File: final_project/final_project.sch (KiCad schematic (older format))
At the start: 35 parts, among them J1 USB_microB_2040002-1, J2 Arduino_ICSP, J3 Conn_01x15_Male, J4 Conn_01x15_Male, U1 FT232RQ, U2 MCP1702T-5002E_CB, U3 TPS2113ADRBR, U4 ATMEGA328PB-MNR, Y1 Crystal

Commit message: full footprints
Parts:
- U2: footprint (none) -> Package_TO_SOT_SMD:SOT-23
- Y1: footprint (none) -> final:CSTNE
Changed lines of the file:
@@
 F 0 "U2" H 4800 2365 50  0000 C CNN
 F 1 "MCP1702T-5002E_CB" H 4800 2274 50  0000 C CNN
-F 2 "" H 4800 2100 50  0001 C CNN
+F 2 "Package_TO_SOT_SMD:SOT-23" H 4800 2100 50  0001 C CNN
 F 3 "" H 4800 2100 50  0001 C CNN
 	1    4800 2000
@@
 F 0 "Y1" V 8654 5331 50  0000 L CNN
 F 1 "Crystal" V 8745 5331 50  0000 L CNN
-F 2 "" H 8700 5200 50  0001 C CNN
+F 2 "final:CSTNE" H 8700 5200 50  0001 C CNN
 F 3 "" H 8700 5200 50  0001 C CNN
 	1    8700 5200

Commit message: add rn symbol
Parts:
- added U?: RN4871, symbol final_project-rescue:RN4871
- S1: footprint (none) -> Button_Switch_SMD:SW_SPST_B3U-1000P
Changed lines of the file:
@@
 F 0 "S1" H 7048 5346 50  0000 L CNN
 F 1 "SW" H 7048 5255 50  0000 L CNN
-F 2 "" V 7050 5400 60  0001 C CNN
+F 2 "Button_Switch_SMD:SW_SPST_B3U-1000P" V 7050 5400 60  0001 C CNN
 F 3 "" V 7050 5400 60  0001 C CNN
 	1    7000 5300
@@
 	1    0    0    -1
 $EndComp
+$Comp
+L final_project-rescue:RN4871 U?
+U 1 1 5CA7B34A
+P 13150 5100
+F 0 "U?" H 13150 5915 50  0000 C CNN
+F 1 "RN4871" H 13150 5824 50  0000 C CNN
+F 2 "" H 13150 5950 50  0001 C CNN
+F 3 "" H 13150 5950 50  0001 C CNN
+	1    13150 5100
+	1    0    0    -1
+$EndComp

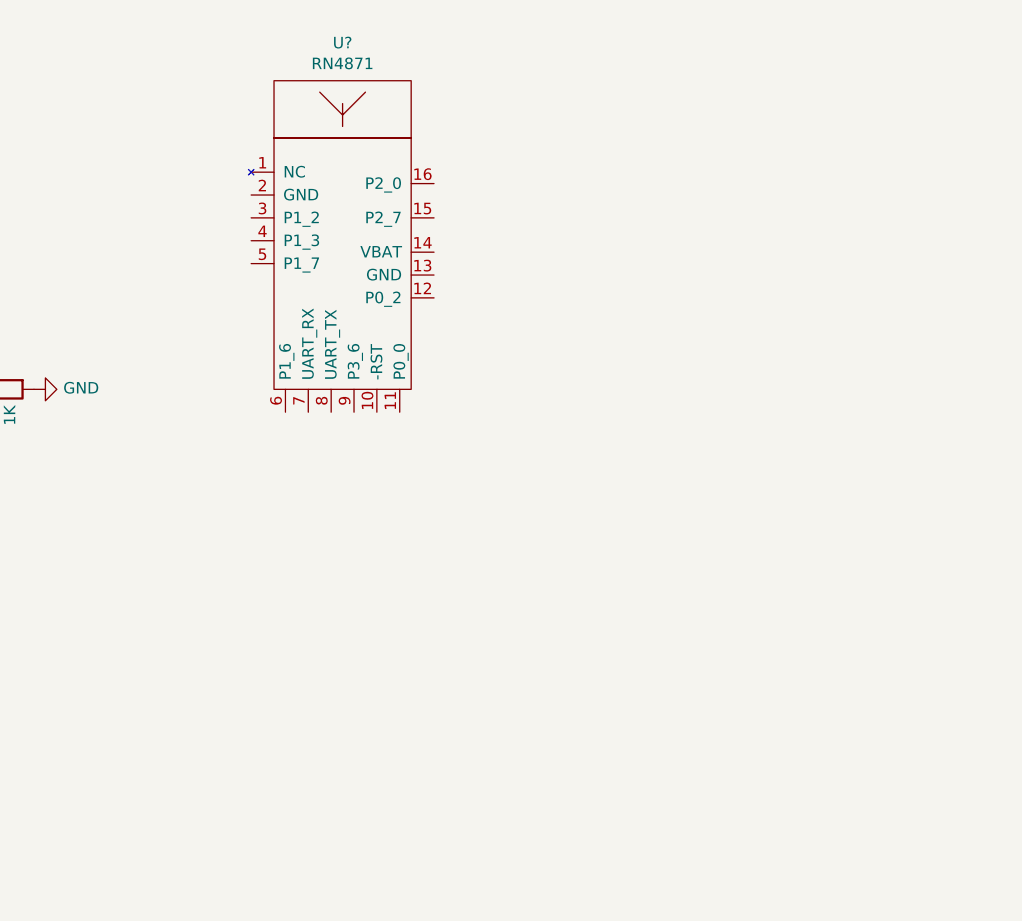
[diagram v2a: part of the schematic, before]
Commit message: rn4871 application circuit
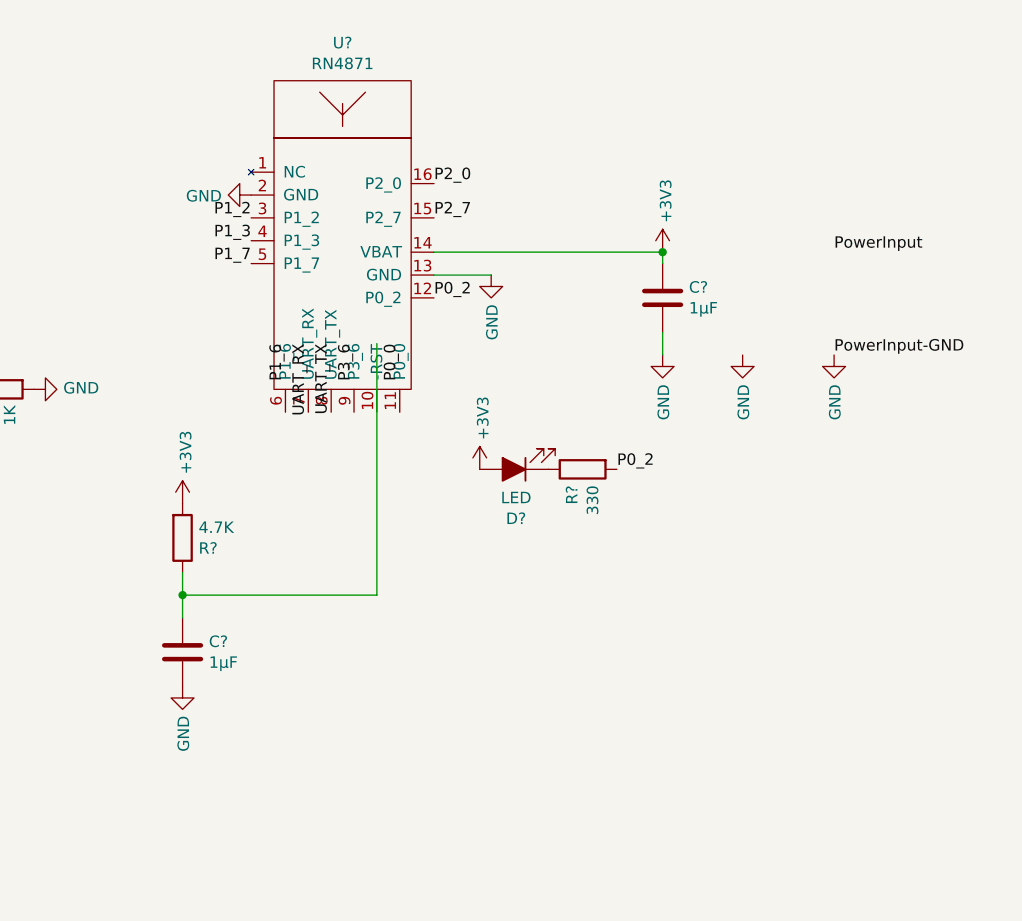
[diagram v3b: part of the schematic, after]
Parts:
- added C? (x2): 1µF, Capacitor_SMD:C_0603_1608Metric, symbol Device:C
- added D?: LED, LED_SMD:LED_0805_2012Metric, symbol Device:LED_ALT
- added R?: 4.7K, Resistor_SMD:R_0603_1608Metric, symbol Device:R
- added R?: 330, Resistor_SMD:R_0603_1608Metric, symbol Device:R
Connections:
- net labels added: P0_0, P0_2, P1_2, P1_3, P1_6, P1_7, P2_0, P2_7, P3_6, PowerInput, PowerInput-GND, UART_RX, UART_TX
- wire segments 98 -> 106
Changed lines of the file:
@@
 	1    0    0    -1
 $EndComp
+$Comp
+L power:GND #PWR?
+U 1 1 5CA7F048
+P 12750 4950
+F 0 "#PWR?" H 12750 4700 50  0001 C CNN
+F 1 "GND" V 12755 4822 50  0000 R CNN
+F 2 "" H 12750 4950 50  0001 C CNN
+F 3 "" H 12750 4950 50  0001 C CNN
+	1    12750 4950
+	0    1    1    0
+$EndComp
+$Comp
+L power:GND #PWR?
+U 1 1 5CA84F44
+P 14550 5650
+F 0 "#PWR?" H 14550 5400 50  0001 C CNN
+F 1 "GND" V 14555 5522 50  0000 R CNN
+F 2 "" H 14550 5650 50  0001 C CNN
+F 3 "" H 14550 5650 50  0001 C CNN
+	1    14550 5650
+	1    0    0    -1
+$EndComp
+Text Label 12750 5050 2    50   ~ 0
+P1_2
+Text Label 12750 5150 2    50   ~ 0
+P1_3
+Text Label 12750 5250 2    50   ~ 0
+P1_7
+Text Label 12900 5600 3    50   ~ 0
+P1_6
+Text Label 13000 5600 3    50   ~ 0
+UART_RX
+Text Label 13100 5600 3    50   ~ 0
+UART_TX
+Text Label 13200 5600 3    50   ~ 0
+P3_6
+Text Label 13400 5600 3    50   ~ 0
+P0_0
+$Comp
+L Device:C C?
+U 1 1 5CA99BD0
+P 12450 6950
+F 0 "C?" H 12565 6996 50  0000 L CNN
+F 1 "1µF" H 12565 6905 50  0000 L CNN
+F 2 "Capacitor_SMD:C_0603_1608Metric" H 12488 6800 50  0001 C CNN
+F 3 "~" H 12450 6950 50  0001 C CNN
+	1    12450 6950
+	1    0    0    -1
+$EndComp
+$Comp
+L power:+3V3 #PWR?
+U 1 1 5CA99BD6
+P 12450 6300
+F 0 "#PWR?" H 12450 6150 50  0001 C CNN
+F 1 "+3V3" V 12465 6428 50  0000 L CNN
+F 2 "" H 12450 6300 50  0001 C CNN
+F 3 "" H 12450 6300 50  0001 C CNN
+	1    12450 6300
+	1    0    0    -1
+$EndComp
+$Comp
+L Device:R R?
+U 1 1 5CAB4E21
+P 12450 6450
+F 0 "R?" H 12520 6496 50  0000 L CNN
+F 1 "4.7K" H 12520 6405 50  0000 L CNN
+F 2 "Resistor_SMD:R_0603_1608Metric" V 12380 6450 50  0001 C CNN
+F 3 "~" H 12450 6450 50  0001 C CNN
+	1    12450 6450
+	1    0    0    1
+$EndComp
+Wire Wire Line
+	12450 6600 12450 6700
+Wire Wire Line
+	12450 6700 13300 6700
+Wire Wire Line
+	13300 6700 13300 5600
+Connection ~ 12450 6700
+Wire Wire Line
+	12450 6700 12450 6800
+$Comp
+L power:GND #PWR?
+U 1 1 5CAC3EE6
+P 12450 7100
+F 0 "#PWR?" H 12450 6850 50  0001 C CNN
+F 1 "GND" V 12455 6972 50  0000 R CNN
+F 2 "" H 12450 7100 50  0001 C CNN
+F 3 "" H 12450 7100 50  0001 C CNN
+	1    12450 7100
+	1    0    0    -1
+$EndComp
+$Comp
+L Device:LED_ALT D?
+U 1 1 5CAD36AD
+P 13900 6150
+F 0 "D?" H 13891 6366 50  0000 C CNN
+F 1 "LED" H 13891 6275 50  0000 C CNN
+F 2 "LED_SMD:LED_0805_2012Metric" H 13900 6150 50  0001 C CNN
+F 3 "~" H 13900 6150 50  0001 C CNN
+	1    13900 6150
+	-1   0    0    1
+$EndComp
+$Comp
+L Device:R R?
+U 1 1 5CAD36B3
+P 14200 6150
+F 0 "R?" H 14270 6196 50  0000 L CNN
+F 1 "330" H 14270 6105 50  0000 L CNN
+F 2 "Resistor_SMD:R_0603_1608Metric" V 14130 6150 50  0001 C CNN
+F 3 "~" H 14200 6150 50  0001 C CNN
+	1    14200 6150
+	0    -1   1    0
+$EndComp
+Text Label 14350 6150 0    50   ~ 0
+P0_2
+$Comp
+L power:+3V3 #PWR?
+U 1 1 5CAD9DD5
+P 13750 6150
+F 0 "#PWR?" H 13750 6000 50  0001 C CNN
+F 1 "+3V3" V 13765 6278 50  0000 L CNN
+F 2 "" H 13750 6150 50  0001 C CNN
+F 3 "" H 13750 6150 50  0001 C CNN
+	1    13750 6150
+	1    0    0    -1
+$EndComp
+$Comp
+L power:GND #PWR?
+U 1 1 5CAE0144
+P 13800 5300
+F 0 "#PWR?" H 13800 5050 50  0001 C CNN
+F 1 "GND" V 13805 5172 50  0000 R CNN
+F 2 "" H 13800 5300 50  0001 C CNN
+F 3 "" H 13800 5300 50  0001 C CNN
+	1    13800 5300
+	1    0    0    -1
+$EndComp
+$Comp
+L power:GND #PWR?
+U 1 1 5CAF2AE5
+P 15300 5650
+F 0 "#PWR?" H 15300 5400 50  0001 C CNN
+F 1 "GND" V 15305 5522 50  0000 R CNN
+F 2 "" H 15300 5650 50  0001 C CNN
+F 3 "" H 15300 5650 50  0001 C CNN
+	1    15300 5650
+	1    0    0    -1
+$EndComp
+$Comp
+L power:GND #PWR?
+U 1 1 5CAF2AEB
+P 14900 5650
+F 0 "#PWR?" H 14900 5400 50  0001 C CNN
+F 1 "GND" V 14905 5522 50  0000 R CNN
+F 2 "" H 14900 5650 50  0001 C CNN
+F 3 "" H 14900 5650 50  0001 C CNN
+	1    14900 5650
+	1    0    0    -1
+$EndComp
+Wire Wire Line
+	13800 5300 13550 5300
+Text Label 13550 5400 0    50   ~ 0
+P0_2
+Text Label 13550 5050 0    50   ~ 0
+P2_7
+Text Label 13550 4900 0    50   ~ 0
+P2_0
+Wire Wire Line
+	14550 5200 13550 5200
+$Comp
+L Device:C C?
+U 1 1 5CB05A4A
+P 14550 5400
+F 0 "C?" H 14665 5446 50  0000 L CNN
+F 1 "1µF" H 14665 5355 50  0000 L CNN
+F 2 "Capacitor_SMD:C_0603_1608Metric" H 14588 5250 50  0001 C CNN
+F 3 "~" H 14550 5400 50  0001 C CNN
+	1    14550 5400
+	1    0    0    -1
+$EndComp
+Wire Wire Line
+	14550 5250 14550 5200
+Wire Wire Line
+	14550 5550 14550 5650
+$Comp
+L power:+3V3 #PWR?
+U 1 1 5CB127B9
+P 14550 5200
+F 0 "#PWR?" H 14550 5050 50  0001 C CNN
+F 1 "+3V3" V 14565 5328 50  0000 L CNN
+F 2 "" H 14550 5200 50  0001 C CNN
+F 3 "" H 14550 5200 50  0001 C CNN
+	1    14550 5200
+	1    0    0    -1
+$EndComp
+Connection ~ 14550 5200
+Text Label 15300 5650 0    50   ~ 0
+PowerInput-GND
+Text Label 15300 5200 0    50   ~ 0
+PowerInput
 $EndSCHEMATC

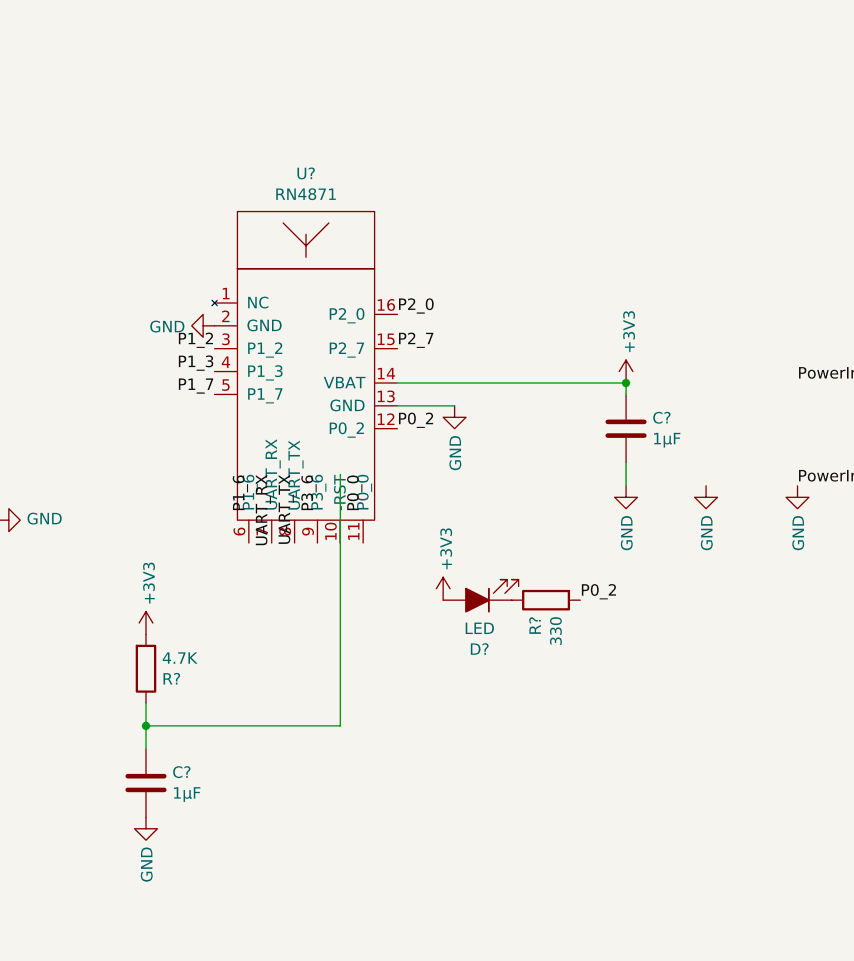
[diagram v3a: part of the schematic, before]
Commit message: add tx LED
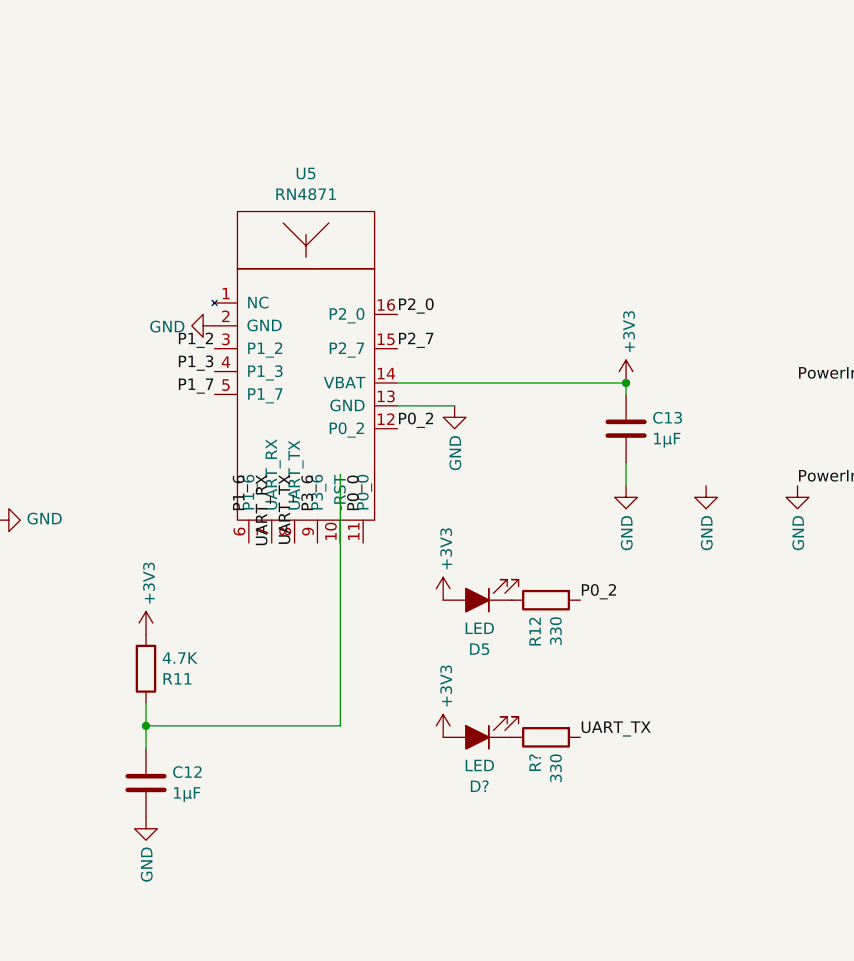
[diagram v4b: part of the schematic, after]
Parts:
- added D?: LED, LED_SMD:LED_0805_2012Metric, symbol Device:LED_ALT
- added R?: 330, Resistor_SMD:R_0603_1608Metric, symbol Device:R
- gave numbers to parts that had none: 6
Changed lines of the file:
@@
 $EndComp
 $Comp
-L final_project-rescue:RN4871 U?
+L final_project-rescue:RN4871 U5
 U 1 1 5CA7B34A
 P 13150 5100
-F 0 "U?" H 13150 5915 50  0000 C CNN
+F 0 "U5" H 13150 5915 50  0000 C CNN
 F 1 "RN4871" H 13150 5824 50  0000 C CNN
 F 2 "" H 13150 5950 50  0001 C CNN
@@
 $EndComp
 $Comp
-L power:GND #PWR?
+L power:GND #PWR0101
 U 1 1 5CA7F048
 P 12750 4950
-F 0 "#PWR?" H 12750 4700 50  0001 C CNN
+F 0 "#PWR0101" H 12750 4700 50  0001 C CNN
 F 1 "GND" V 12755 4822 50  0000 R CNN
 F 2 "" H 12750 4950 50  0001 C CNN
@@
 $EndComp
 $Comp
-L power:GND #PWR?
+L power:GND #PWR0102
 U 1 1 5CA84F44
 P 14550 5650
-F 0 "#PWR?" H 14550 5400 50  0001 C CNN
+F 0 "#PWR0102" H 14550 5400 50  0001 C CNN
 F 1 "GND" V 14555 5522 50  0000 R CNN
 F 2 "" H 14550 5650 50  0001 C CNN
@@
 P0_0
 $Comp
-L Device:C C?
+L Device:C C12
 U 1 1 5CA99BD0
 P 12450 6950
-F 0 "C?" H 12565 6996 50  0000 L CNN
+F 0 "C12" H 12565 6996 50  0000 L CNN
 F 1 "1µF" H 12565 6905 50  0000 L CNN
 F 2 "Capacitor_SMD:C_0603_1608Metric" H 12488 6800 50  0001 C CNN
@@
 $EndComp
 $Comp
-L power:+3V3 #PWR?
+L power:+3V3 #PWR0103
 U 1 1 5CA99BD6
 P 12450 6300
-F 0 "#PWR?" H 12450 6150 50  0001 C CNN
+F 0 "#PWR0103" H 12450 6150 50  0001 C CNN
 F 1 "+3V3" V 12465 6428 50  0000 L CNN
 F 2 "" H 12450 6300 50  0001 C CNN
@@
 $EndComp
 $Comp
-L Device:R R?
+L Device:R R11
 U 1 1 5CAB4E21
 P 12450 6450
-F 0 "R?" H 12520 6496 50  0000 L CNN
+F 0 "R11" H 12520 6496 50  0000 L CNN
 F 1 "4.7K" H 12520 6405 50  0000 L CNN
 F 2 "Resistor_SMD:R_0603_1608Metric" V 12380 6450 50  0001 C CNN
@@
 	12450 6700 12450 6800
 $Comp
-L power:GND #PWR?
+L power:GND #PWR0104
 U 1 1 5CAC3EE6
 P 12450 7100
-F 0 "#PWR?" H 12450 6850 50  0001 C CNN
+F 0 "#PWR0104" H 12450 6850 50  0001 C CNN
 F 1 "GND" V 12455 6972 50  0000 R CNN
 F 2 "" H 12450 7100 50  0001 C CNN
@@
 $EndComp
 $Comp
-L Device:LED_ALT D?
+L Device:LED_ALT D5
 U 1 1 5CAD36AD
 P 13900 6150
-F 0 "D?" H 13891 6366 50  0000 C CNN
+F 0 "D5" H 13891 6366 50  0000 C CNN
 F 1 "LED" H 13891 6275 50  0000 C CNN
 F 2 "LED_SMD:LED_0805_2012Metric" H 13900 6150 50  0001 C CNN
@@
 $EndComp
 $Comp
-L Device:R R?
+L Device:R R12
 U 1 1 5CAD36B3
 P 14200 6150
-F 0 "R?" H 14270 6196 50  0000 L CNN
+F 0 "R12" H 14270 6196 50  0000 L CNN
 F 1 "330" H 14270 6105 50  0000 L CNN
 F 2 "Resistor_SMD:R_0603_1608Metric" V 14130 6150 50  0001 C CNN
@@
 P0_2
 $Comp
-L power:+3V3 #PWR?
+L power:+3V3 #PWR0105
 U 1 1 5CAD9DD5
 P 13750 6150
-F 0 "#PWR?" H 13750 6000 50  0001 C CNN
+F 0 "#PWR0105" H 13750 6000 50  0001 C CNN
 F 1 "+3V3" V 13765 6278 50  0000 L CNN
 F 2 "" H 13750 6150 50  0001 C CNN
@@
 $EndComp
 $Comp
-L power:GND #PWR?
+L power:GND #PWR0106
 U 1 1 5CAE0144
 P 13800 5300
-F 0 "#PWR?" H 13800 5050 50  0001 C CNN
+F 0 "#PWR0106" H 13800 5050 50  0001 C CNN
 F 1 "GND" V 13805 5172 50  0000 R CNN
 F 2 "" H 13800 5300 50  0001 C CNN
@@
 $EndComp
 $Comp
-L power:GND #PWR?
+L power:GND #PWR0107
 U 1 1 5CAF2AE5
 P 15300 5650
-F 0 "#PWR?" H 15300 5400 50  0001 C CNN
+F 0 "#PWR0107" H 15300 5400 50  0001 C CNN
 F 1 "GND" V 15305 5522 50  0000 R CNN
 F 2 "" H 15300 5650 50  0001 C CNN
@@
 $EndComp
 $Comp
-L power:GND #PWR?
+L power:GND #PWR0108
 U 1 1 5CAF2AEB
 P 14900 5650
-F 0 "#PWR?" H 14900 5400 50  0001 C CNN
+F 0 "#PWR0108" H 14900 5400 50  0001 C CNN
 F 1 "GND" V 14905 5522 50  0000 R CNN
 F 2 "" H 14900 5650 50  0001 C CNN
@@
 	14550 5200 13550 5200
 $Comp
-L Device:C C?
+L Device:C C13
 U 1 1 5CB05A4A
 P 14550 5400
-F 0 "C?" H 14665 5446 50  0000 L CNN
+F 0 "C13" H 14665 5446 50  0000 L CNN
 F 1 "1µF" H 14665 5355 50  0000 L CNN
 F 2 "Capacitor_SMD:C_0603_1608Metric" H 14588 5250 50  0001 C CNN
@@
 	14550 5550 14550 5650
 $Comp
-L power:+3V3 #PWR?
+L power:+3V3 #PWR0109
 U 1 1 5CB127B9
 P 14550 5200
-F 0 "#PWR?" H 14550 5050 50  0001 C CNN
+F 0 "#PWR0109" H 14550 5050 50  0001 C CNN
 F 1 "+3V3" V 14565 5328 50  0000 L CNN
 F 2 "" H 14550 5200 50  0001 C CNN
@@
 Text Label 15300 5200 0    50   ~ 0
 PowerInput
+$Comp
+L Device:LED_ALT D?
+U 1 1 5CB1F09B
+P 13900 6750
+F 0 "D?" H 13891 6966 50  0000 C CNN
+F 1 "LED" H 13891 6875 50  0000 C CNN
+F 2 "LED_SMD:LED_0805_2012Metric" H 13900 6750 50  0001 C CNN
+F 3 "~" H 13900 6750 50  0001 C CNN
+	1    13900 6750
+	-1   0    0    1
+$EndComp
+$Comp
+L Device:R R?
+U 1 1 5CB1F0A1
+P 14200 6750
+F 0 "R?" H 14270 6796 50  0000 L CNN
+F 1 "330" H 14270 6705 50  0000 L CNN
+F 2 "Resistor_SMD:R_0603_1608Metric" V 14130 6750 50  0001 C CNN
+F 3 "~" H 14200 6750 50  0001 C CNN
+	1    14200 6750
+	0    -1   1    0
+$EndComp
+Text Label 14350 6750 0    50   ~ 0
+UART_TX
+$Comp
+L power:+3V3 #PWR?
+U 1 1 5CB1F0A8
+P 13750 6750
+F 0 "#PWR?" H 13750 6600 50  0001 C CNN
+F 1 "+3V3" V 13765 6878 50  0000 L CNN
+F 2 "" H 13750 6750 50  0001 C CNN
+F 3 "" H 13750 6750 50  0001 C CNN
+	1    13750 6750
+	1    0    0    -1
+$EndComp
 $EndSCHEMATC

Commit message: update schematic
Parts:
- removed C12: 1µF, Capacitor_SMD:C_0603_1608Metric, symbol Device:C
- removed D5: LED, LED_SMD:LED_0805_2012Metric, symbol Device:LED_ALT
- removed J3, J4: Conn_01x15_Male, Connector_PinSocket_2.54mm:PinSocket_1x15_P2.54mm_Vertical, symbol Connector:Conn_01x15_Male
- removed R12: 330, Resistor_SMD:R_0603_1608Metric, symbol Device:R
- added C? (x2): 1µF, Capacitor_SMD:C_0603_1608Metric, symbol Device:C
- added D? (x3): LED, LED_SMD:LED_0805_2012Metric, symbol Device:LED_ALT
- added J?: Conn_01x06_Male, symbol Connector:Conn_01x06_Male
- added R? (x3): 330, Resistor_SMD:R_0603_1608Metric, symbol Device:R
- added S?: SW, Button_Switch_SMD:SW_SPST_B3U-1000P, symbol final_project-rescue:SW-final_project
- added U?: ISM330DLC, symbol final_project-rescue:ISM330DLC
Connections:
- net labels added: ArduinoTransmit, GNDorVdd, LowBatt, PowerOn, RF_Active
- net labels removed: P0_0, P0_2, P1_2, P1_3, P1_6, P1_7, P2_0, P2_7, P3_6, PowerInput, PowerInput-GND, UART_RX, UART_TX
- wire segments 106 -> 111
- no-connect marks 25 -> 26
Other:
- moved on the sheet: C13, D?, J2, R11, R?, U5

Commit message: new schmeatic
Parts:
- added C15, C16: 10µF, Capacitor_SMD:C_0805_2012Metric, symbol Device:C
- added R12, R13, R14, R15, R16: 1K, Resistor_SMD:R_0603_1608Metric, symbol Device:R
- added U10, U7, U8, U9: MAX14870, symbol final_project-rescue:MAX14870
- gave numbers to parts that had none: 13
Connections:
- net +5V: now also R14.1
- net A1: now also U6.12 (CS); no longer U5.4 (P1_3)
- net A4: now also U6.14 (SDA)
- net A5: now also U6.13 (SCC), U10.6 (DIR), U7.6 (DIR), U8.6 (DIR), U9.6 (DIR)
- net A6: now also R14.2, U10.7 (~FAULT), U7.7 (~FAULT), U8.7 (~FAULT), U9.7 (~FAULT)
- net D10: now also U10.5 (PWM), U8.5 (PWM); no longer U6.13 (SCC)
- net D7: now also U5.4 (P1_3); no longer U6.14 (SDA)
- net D9: now also U7.5 (PWM), U9.5 (PWM); no longer U6.12 (CS)
- net GND: now also C15.2, C16.2, R12.2, R13.2, R15.2, R16.2, U10.13 (GND_(PAD)), U10.8 (~EN), U10.9 (GND), U7.13 (GND_(PAD)), U7.8 (~EN), U7.9 (GND), U8.13 (GND_(PAD)), U8.8 (~EN), U8.9 (GND), U9.13 (GND_(PAD)), U9.8 (~EN), U9.9 (GND)
- net A2: no longer names the net of U4.25 (PC2/ADC2)
- net A3: no longer names the net of U4.26 (PC3/ADC3)
- new net: R12.1, U7.1 (COM), U7.12 (COM), U7.4 (SNS)
- new net: R15.1, U9.1 (COM), U9.12 (COM), U9.4 (SNS)
- new net: R13.1, U8.1 (COM), U8.12 (COM), U8.4 (SNS)
- new net: R16.1, U10.1 (COM), U10.12 (COM), U10.4 (SNS)
- new net +BATT: C15.1, C16.1, U10.10 (VDD), U10.3 (VDD), U7.10 (VDD), U7.3 (VDD), U8.10 (VDD), U8.3 (VDD), U9.10 (VDD), U9.3 (VDD)
- new net motor1a: U7.2 (M1)
- new net motor1b: U7.11 (M2)
- new net motor2a: U9.2 (M1)
- new net motor2b: U9.11 (M2)
- new net motor3a: U8.2 (M1)
- new net motor3b: U8.11 (M2)
- new net motor4a: U10.2 (M1)
- new net motor4b: U10.11 (M2)
- no-connect marks 26 -> 28
